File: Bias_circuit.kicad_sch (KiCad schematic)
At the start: 55 parts, among them Q3 BC846, Q4 BC846, Q5 PMOS, U5 LM723_DIP14

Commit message: Add files via upload
Fixed DRC shorted nets error
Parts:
- removed Q5: PMOS, Package_TO_SOT_SMD:SOT-23, symbol Simulation_SPICE:PMOS
- added Q5: AO3400A, Package_TO_SOT_SMD:SOT-23, symbol Transistor_FET:AO3400A
- renumbered C51 to C53, C52 to C54, C53 to C55, C54 to C56, C55 to C57, C56 to C58, C57 to C59, C58 to C60, C59 to C61, C60 to C62, C61 to C63, C62 to C64, C63 to C65, C64 to C66, C65 to C67, C66 to C68, C67 to C69, C68 to C70, C69 to C71, C70 to C72, C71 to C73, D16 to D18, R29 to R27, R30 to R28, R31 to R29, R32 to R30, R33 to R31, R34 to R32, R35 to R33, R36 to R34, R37 to R35, R38 to R36, R39 to R37, R40 to R38, R41 to R39, R42 to R40, R43 to R41, R44 to R42, R45 to R43, R46 to R44, R47 to R45, R48 to R46, R49 to R47, R50 to R48, RV4 to RV2, RV5 to RV3, RV6 to RV4, RV7 to RV5, U5 to U3
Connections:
- net +12V: now also Q5.3 (D)
- net at Q3.3 (C), R29.2: now also Q5.1 (G)
- net at R31.1: now also Q5.2 (S)
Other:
- moved on the sheet: C56

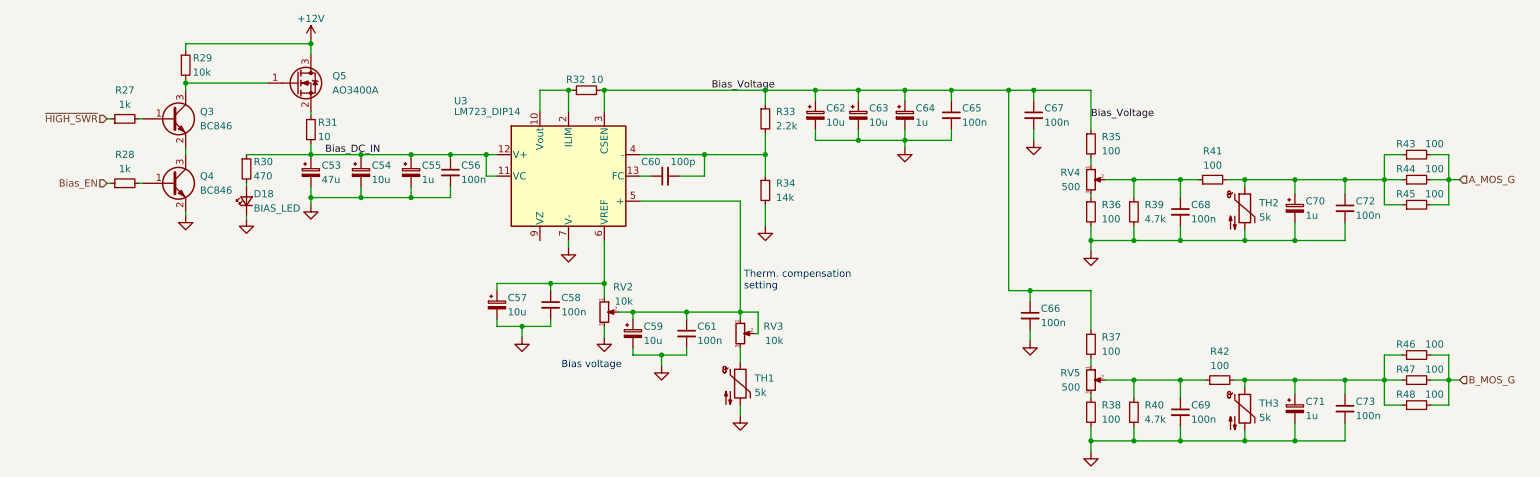
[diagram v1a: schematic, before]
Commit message: Used ERC on PA-Deck Schematic
Initially many hundreds of warnings, and some errors.
Apart from 8 exclusions These have all largely been fixed.
Many Symbols required updating from the appropriate library, but mostly a huge number or warnings about "symbol pin or wire end off grid connection".  Took a while, but I figured out what the problem is.
L5 & L6 exclusion referred to a TXRX library that wasn't available.
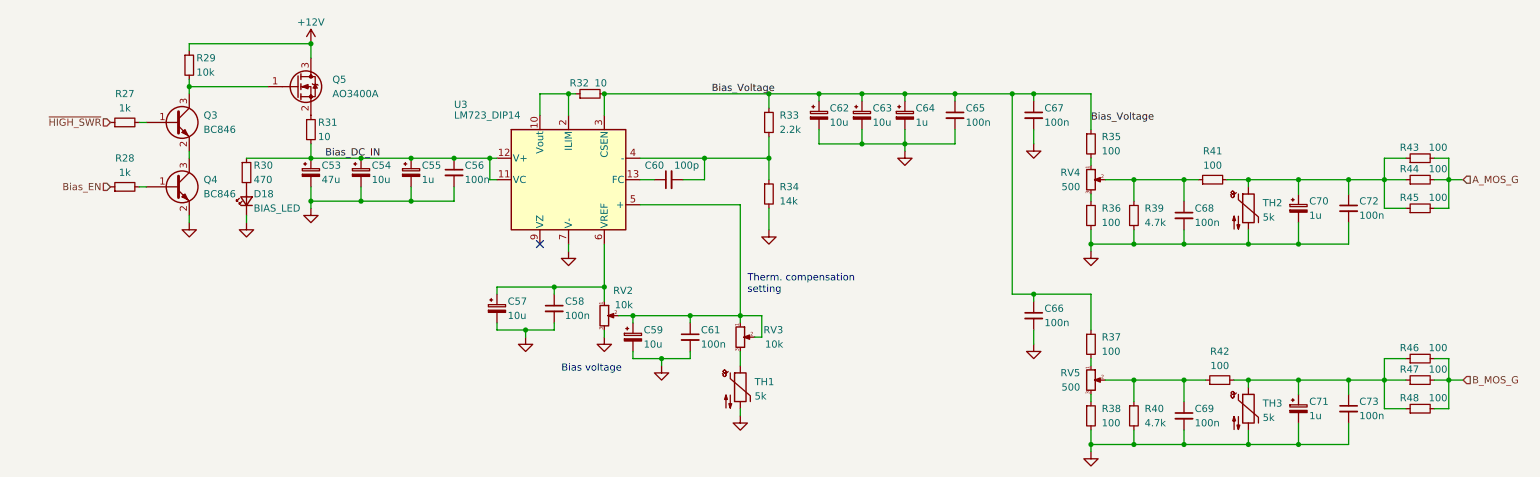
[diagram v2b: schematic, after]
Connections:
- no-connect marks 0 -> 1
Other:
- moved on the sheet: C56, C57, C58, C59, C60, C61, C62, C63, C65, C66, C68, C69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

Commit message: Ready to Order
Applied minor changes in preparation to order CPBs and components.
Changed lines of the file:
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@@
+	(wire
+		(pts
+			(xy 120.65 84.455) (xy 138.43 84.455)
+		)
+		(stroke
+			(width 0)
+			(type default)
+		)
+	)
 	(wire
 		(pts
@@
 	(wire
 		(pts
-			(xy 138.43 104.14) (xy 138.43 84.455)
-		)
-		(stroke
-			(width 0)
-			(type default)
-		)
-	)
-	(wire
-		(pts
 			(xy 152.4 64.77) (xy 152.4 66.04)
 		)
@@
 	(wire
 		(pts
+			(xy 138.43 84.455) (xy 138.43 104.14)
+		)
+		(stroke
+			(width 0)
+			(type default)
+		)
+	)
+	(wire
+		(pts
 			(xy 95.25 106.68) (xy 95.25 105.41)
 		)
@@
 		)
 		(stroke
-			(width 0)
-			(type default)
-		)
-	)
-	(wire
-		(pts
-			(xy 138.43 84.455) (xy 120.65 84.455)
-		)
-		(stroke
